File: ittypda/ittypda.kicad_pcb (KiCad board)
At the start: 2 copper layers, 105 x 109.8 mm, 154 parts, among them CN1 S2B-PH-SM4-TB, J1 USB_C_Receptacle_USB2.0_14P, J13 Conn_01x05_Pin, J14 Conn_01x05_Pin, J2 Conn_01x04_Pin, SW1 Switch, SW10 Switch, SW11 Switch, SW12 Switch, SW13 Switch, SW14 Switch, SW15 Switch, SW16 Switch, SW17 Switch, SW18 Switch, SW19 Switch, SW2 Switch, SW20 Switch, SW21 Switch, SW22 Switch, SW23 Switch, SW24 Switch, SW25 SLIDE SWITCH, SW26 Switch, SW27 Switch, SW28 Switch, SW29 Switch, SW3 Switch, SW30 Switch, SW31 Switch, SW32 Switch, SW33 Switch, SW34 Switch, SW36 Switch, SW37 Switch, SW38 Switch, SW39 Switch, SW4 Switch, SW41 Switch, SW42 Switch, SW43 Switch, SW44 Switch, SW45 Switch, SW46 Switch, SW47 Switch, SW48 Switch, SW49 Switch, SW5 Switch, SW50 Switch, SW51 Switch, SW52 Switch, SW53 Switch, SW54 Switch, SW55 Switch, SW56 Switch, SW57 Switch, SW58 Switch, SW59 Switch, SW6 Switch, SW60 Switch, SW61 Switch, SW7 Switch, SW8 Switch, SW9 Switch, U1 STM32F401RETx, U2 BQ24040DSQR, U3 TLV75801PDRV, Y1 16Mhz

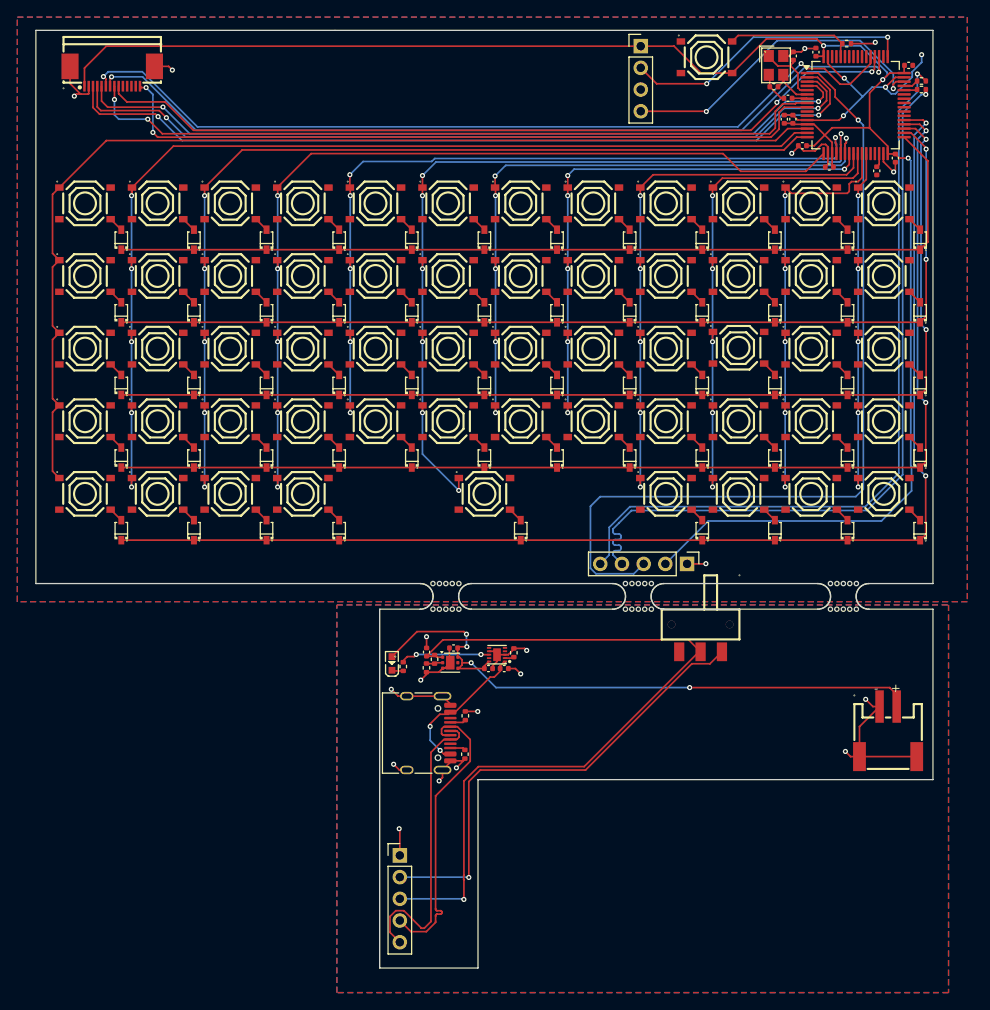
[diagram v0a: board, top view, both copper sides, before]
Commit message: change microcontroller to the STM32F411RET6
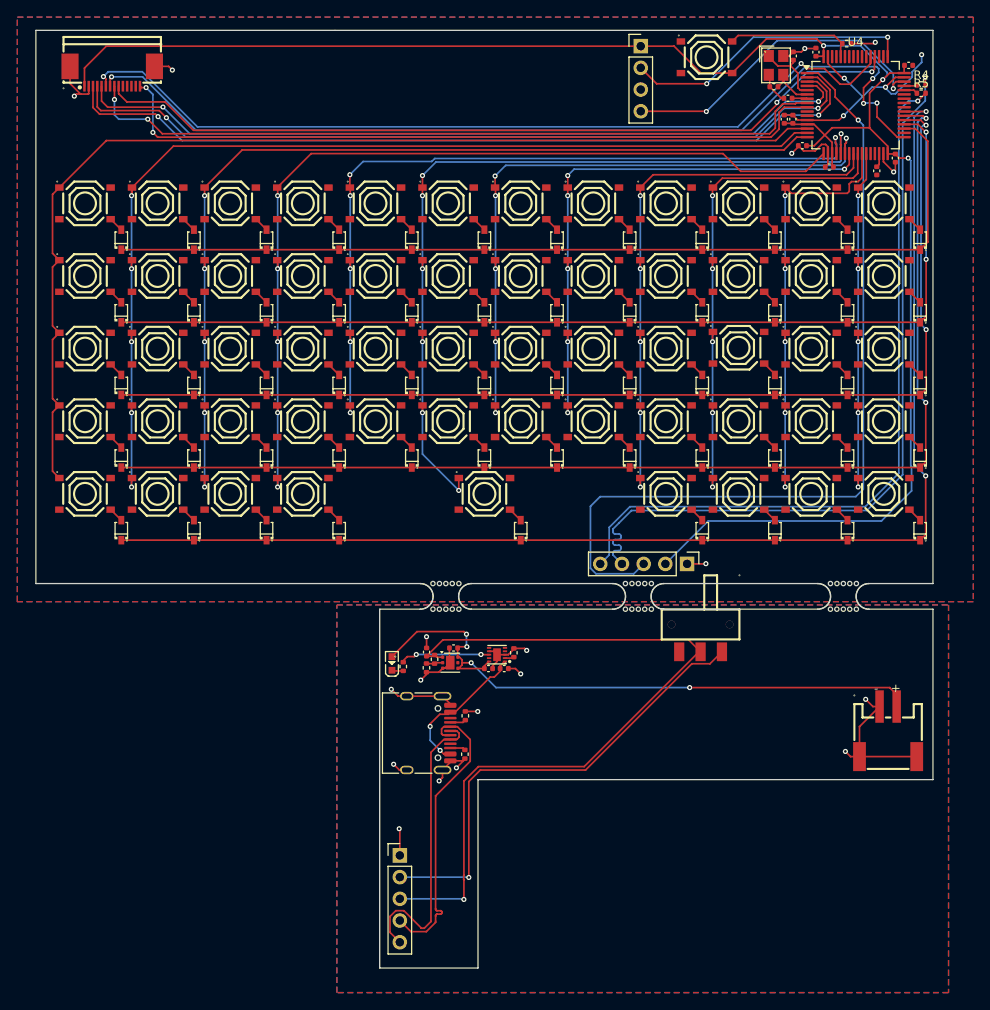
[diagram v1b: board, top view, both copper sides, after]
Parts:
- removed U1: STM32F401RETx, Package_QFP:LQFP-64_10x10mm_P0.5mm
- added U4: STM32F411RETx, Package_QFP:LQFP-64_10x10mm_P0.5mm, F.Cu at (120.0, 39.5)
- moved R5 1.43 mm to (127.6, 38.1)
- moved R4 0.53 mm to (127.6, 37.1)
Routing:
- net SCK: track 99.1 -> 108.9 mm, vias 2 -> 4
- net InD-: track 90.2 -> 87.6 mm
- net InD+: track 90.3 -> 92.5 mm
- net Row0: track 108.2 -> 110.0 mm
- net Row3: track 136.9 -> 138.6 mm
- net Row2: track 127.3 -> 128.9 mm
- net Row1: track 117.5 -> 119.0 mm
- net Row4: track 146.4 -> 147.8 mm

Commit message: update pcb with new cap values
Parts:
- C10: value 100uF -> 1uF
- C15: value 0.1uF -> 100nF
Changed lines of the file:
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@@
 			)
 		)
-		(property "Value" "0.1uF"
+		(property "Value" "100nF"
 			(at 0 1.16 0)
 			(layer "F.Fab")
@@
 			)
 		)
-		(property "Value" "100uF"
+		(property "Value" "1uF"
 			(at 0 1.16 90)
 			(layer "F.Fab")

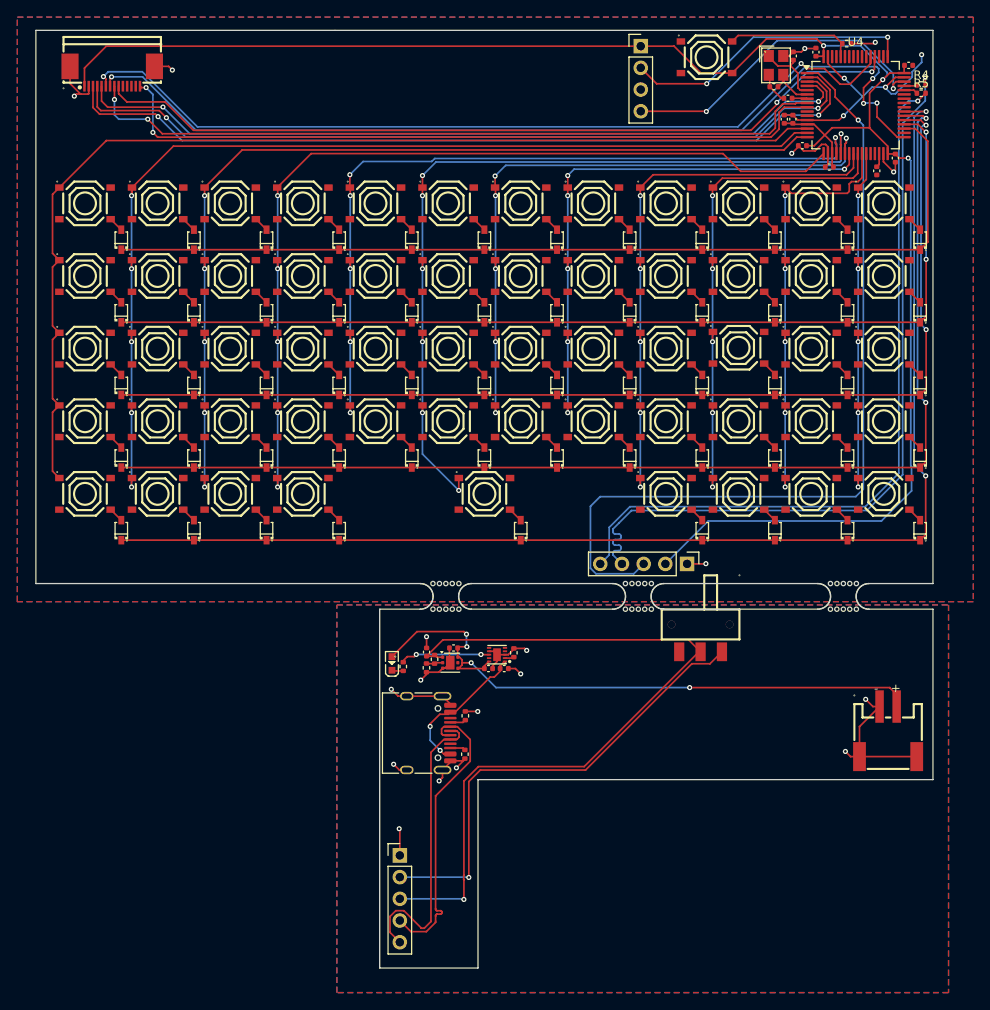
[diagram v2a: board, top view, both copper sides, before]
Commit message: move boot0 button and repair edge cuts
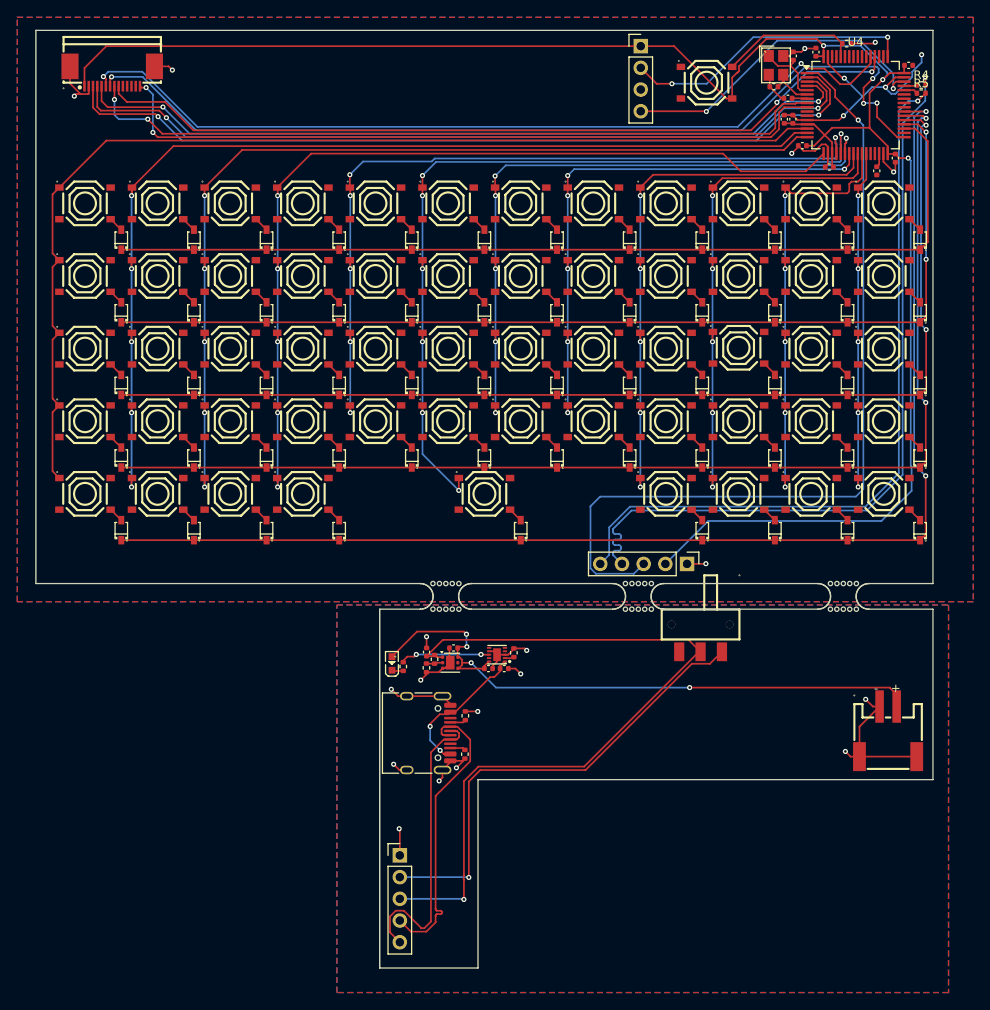
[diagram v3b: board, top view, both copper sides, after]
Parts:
- moved SW61 2.98 mm to (102.5, 36.9)
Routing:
- net +3.3V: track 210.7 -> 215.0 mm
- net Net-(SW61-B): track 15.2 -> 16.4 mm
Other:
- outline, holes or cut-outs redrawn

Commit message: add silkscreen art !!
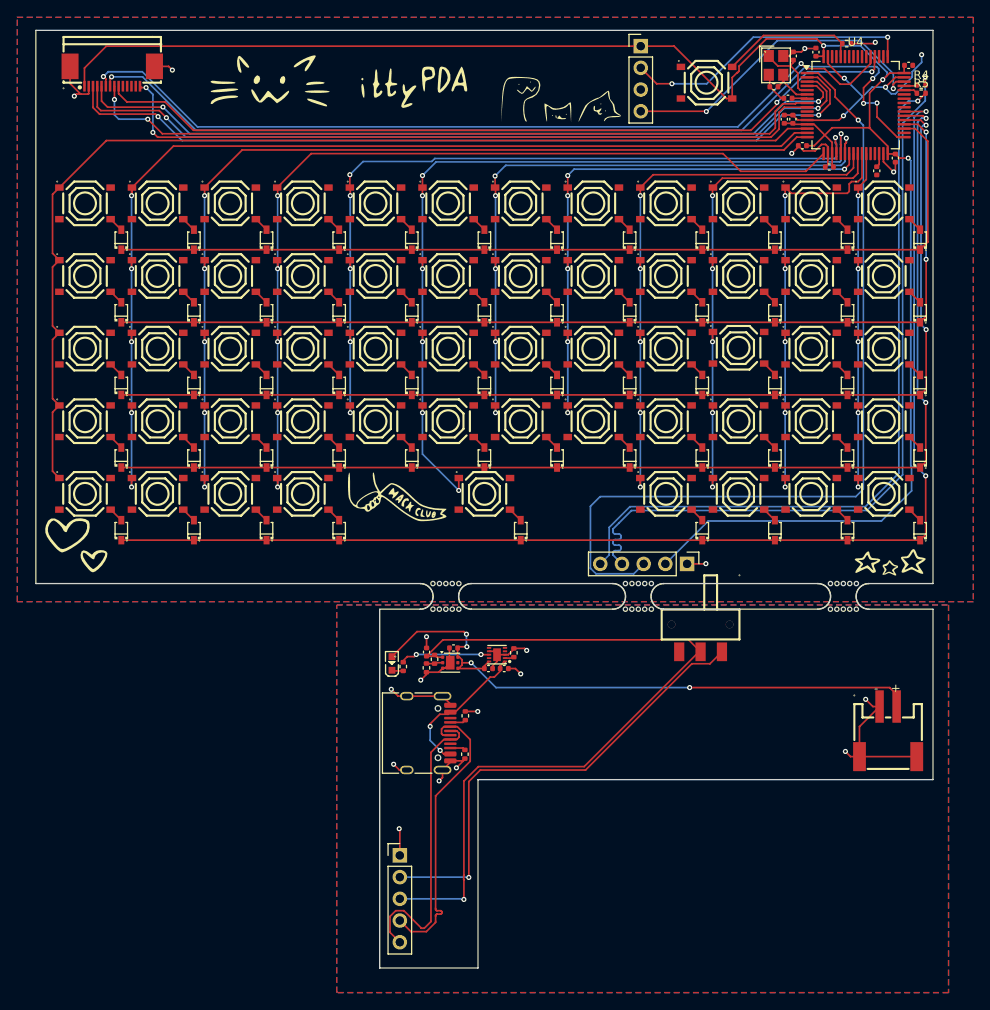
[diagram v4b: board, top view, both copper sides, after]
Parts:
- added G***: LOGO, silkscreen:stars, F.Cu at (124.0, 93.0)
- added G***: LOGO, silkscreen:cats, F.Cu at (85.5, 38.8)
- added G***: LOGO, silkscreen:flag, F.Cu at (66.3, 85.3)
- added G***: LOGO, silkscreen:logo, F.Cu at (59.5, 36.8)
- added G***: LOGO, silkscreen:hearts, F.Cu at (28.7, 91.0)
- added G***: LOGO, silkscreen:bend, B.Cu at (54.1, 63.2)

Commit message: even out usb data lines
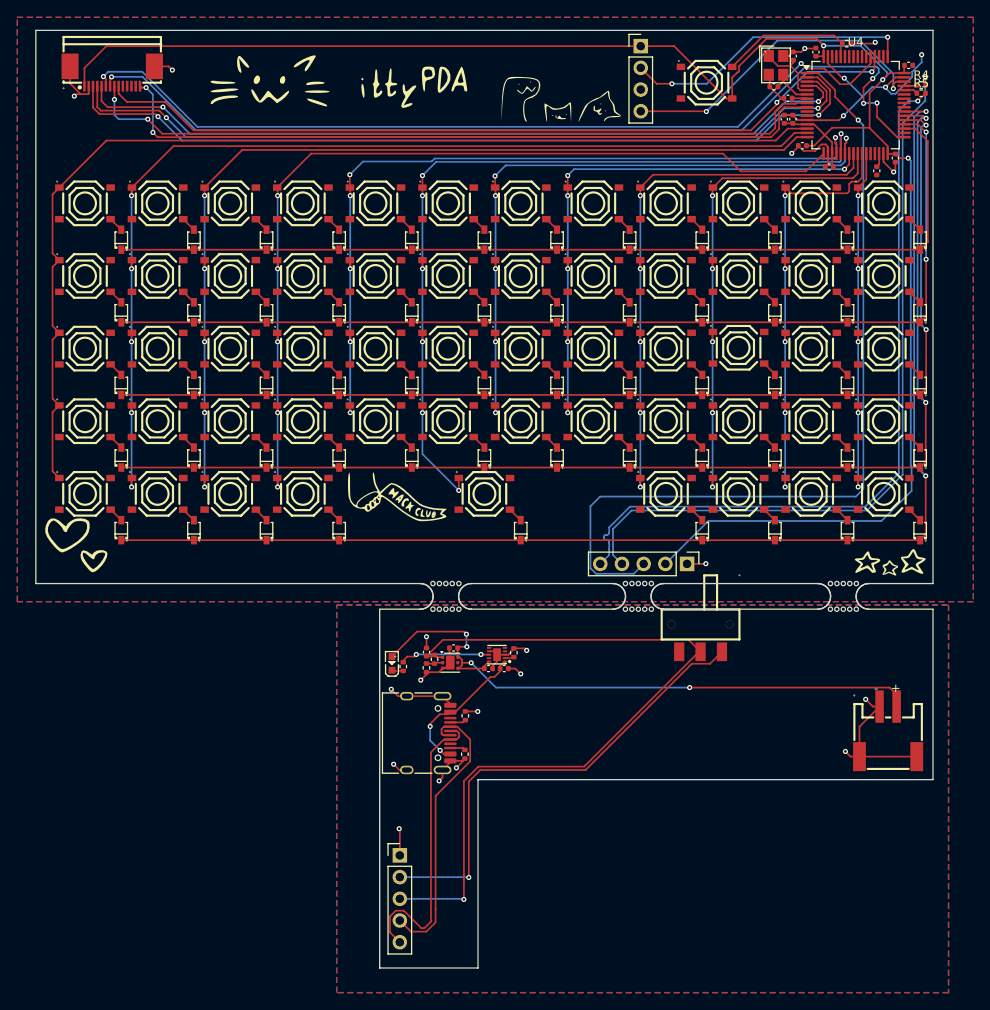
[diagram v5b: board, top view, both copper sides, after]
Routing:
- net InD+: track 92.5 -> 89.7 mm
- net OutD+: track 35.2 -> 34.0 mm
- net InD-: track 87.6 -> 88.4 mm

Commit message: label all header pins and move boot0 button slightly
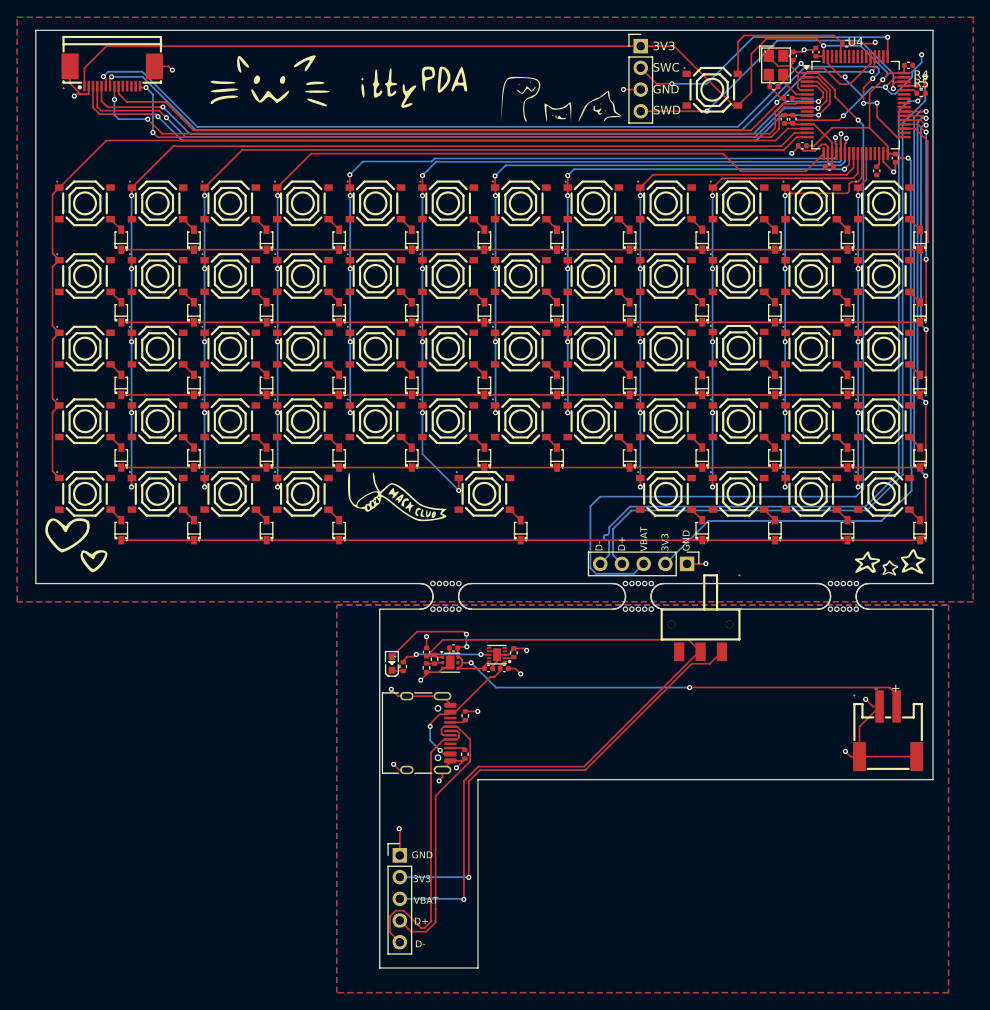
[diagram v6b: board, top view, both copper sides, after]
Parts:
- moved SW61 1.07 mm to (103.2, 37.7)
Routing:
- net GND: track 117.8 -> 120.0 mm, vias 23 -> 24
- net Net-(SW61-B): track 16.4 -> 18.3 mm
- net +3.3V: track 215.0 -> 216.5 mm
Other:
- board text added: "3V3"
- board text added: "D+"
- board text added: "D-"
- board text added: "GND"
- board text added: "SWC"
- board text added: "SWD"
- board text added: "VBAT"

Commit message: updated 'dont bend' art
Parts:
- moved G*** 3.03 mm to (54.7, 66.2)
